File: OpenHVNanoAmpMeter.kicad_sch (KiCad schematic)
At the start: 0 parts

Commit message: updated structure
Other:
- sheet CurrentMeasurement ports: added TIA_IN; removed none
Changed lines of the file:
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@@
 (kicad_sch (version 20211123) (generator eeschema)
   (paper "A4")
-  (sheet (at 154.94 67.31) (size 73.66 34.29) (fields_autoplaced)
+  (sheet (at 50.8 50.8) (size 29.21 34.29) (fields_autoplaced)
     (stroke (width 0.1524) (type solid) (color 0 0 0 0))
     (fill (color 0 0 0 0.0000))
-    (property "Sheet name" "CurrentMeasurement" (id 0) (at 154.94 66.5984 0)
+    (property "Sheet name" "CurrentMeasurement" (id 0) (at 50.8 50.0884 0)
       (effects (font (size 1.27 1.27)) (justify left bottom))
     )
-    (property "Sheet file" "CurrentMeasurement.kicad_sch" (id 1) (at 154.94 102.1846 0)
+    (property "Sheet file" "CurrentMeasurement.kicad_sch" (id 1) (at 50.8 85.6746 0)
       (effects (font (size 1.27 1.27)) (justify left top) hide)
+    )
+    (pin "TIA_IN" input (at 50.8 59.69 180)
+      (effects (font (size 1.27 1.27)) (justify left))
     )
   )
@@
     )
     (property "Sheet file" "InterfacePCside.kicad_sch" (id 1) (at 22.86 36.1446 0)
-      (effects (font (size 1.27 1.27)) (justify left top))
+      (effects (font (size 1.27 1.27)) (justify left top) hide)
     )
   )
-  (sheet (at 105.41 64.77) (size 24.13 41.91) (fields_autoplaced)
+  (sheet (at 87.63 50.8) (size 24.13 34.29) (fields_autoplaced)
     (stroke (width 0.1524) (type solid) (color 0 0 0 0))
     (fill (color 0 0 0 0.0000))
-    (property "Sheet name" "DataProcessing" (id 0) (at 105.41 64.0584 0)
+    (property "Sheet name" "DataProcessing" (id 0) (at 87.63 50.0884 0)
       (effects (font (size 1.27 1.27)) (justify left bottom))
     )
-    (property "Sheet file" "DataProcessing.kicad_sch" (id 1) (at 105.41 107.2646 0)
-      (effects (font (size 1.27 1.27)) (justify left top))
+    (property "Sheet file" "DataProcessing.kicad_sch" (id 1) (at 87.63 85.6746 0)
+      (effects (font (size 1.27 1.27)) (justify left top) hide)
     )
   )
-  (sheet (at 69.85 66.04) (size 27.94 30.48) (fields_autoplaced)
+  (sheet (at 119.38 50.8) (size 27.94 34.29) (fields_autoplaced)
     (stroke (width 0.1524) (type solid) (color 0 0 0 0))
     (fill (color 0 0 0 0.0000))
-    (property "Sheet name" "Interface" (id 0) (at 69.85 65.3284 0)
+    (property "Sheet name" "Interface" (id 0) (at 119.38 50.0884 0)
       (effects (font (size 1.27 1.27)) (justify left bottom))
     )
-    (property "Sheet file" "Interface.kicad_sch" (id 1) (at 69.85 97.1046 0)
-      (effects (font (size 1.27 1.27)) (justify left top))
+    (property "Sheet file" "Interface.kicad_sch" (id 1) (at 119.38 85.6746 0)
+      (effects (font (size 1.27 1.27)) (justify left top) hide)
     )
   )
@@
   )
   (symbol_instances
+    (path "/1a416e56-70b9-4536-9e9f-d6906909692e/55690313-1407-4934-afe0-4c27694f0ce2"
+      (reference "#PWR?") (unit 1) (value "GND1") (footprint "")
+    )
+    (path "/1a416e56-70b9-4536-9e9f-d6906909692e/2dff8e7c-3323-45f1-b4d6-142a477025b9"
+      (reference "C?") (unit 1) (value "C") (footprint "")
+    )
+    (path "/1a416e56-70b9-4536-9e9f-d6906909692e/7952f13c-ca8e-4d9a-ae66-7db9acc3a740"
+      (reference "R?") (unit 1) (value "R") (footprint "")
+    )
     (path "/1a416e56-70b9-4536-9e9f-d6906909692e/7889dd03-e008-429e-85c1-51a59a2503fb"
       (reference "U?") (unit 1) (value "TLC272") (footprint "")
     )
-    (path "/1a416e56-70b9-4536-9e9f-d6906909692e/fbe6d585-7b11-4a8d-a098-4cf5a74e9a83"
-      (reference "U?") (unit 2) (value "TLC272") (footprint "")
-    )
     (path "/1a416e56-70b9-4536-9e9f-d6906909692e/d047c0e9-8f92-47b0-ac3f-1065bf5fbcc0"

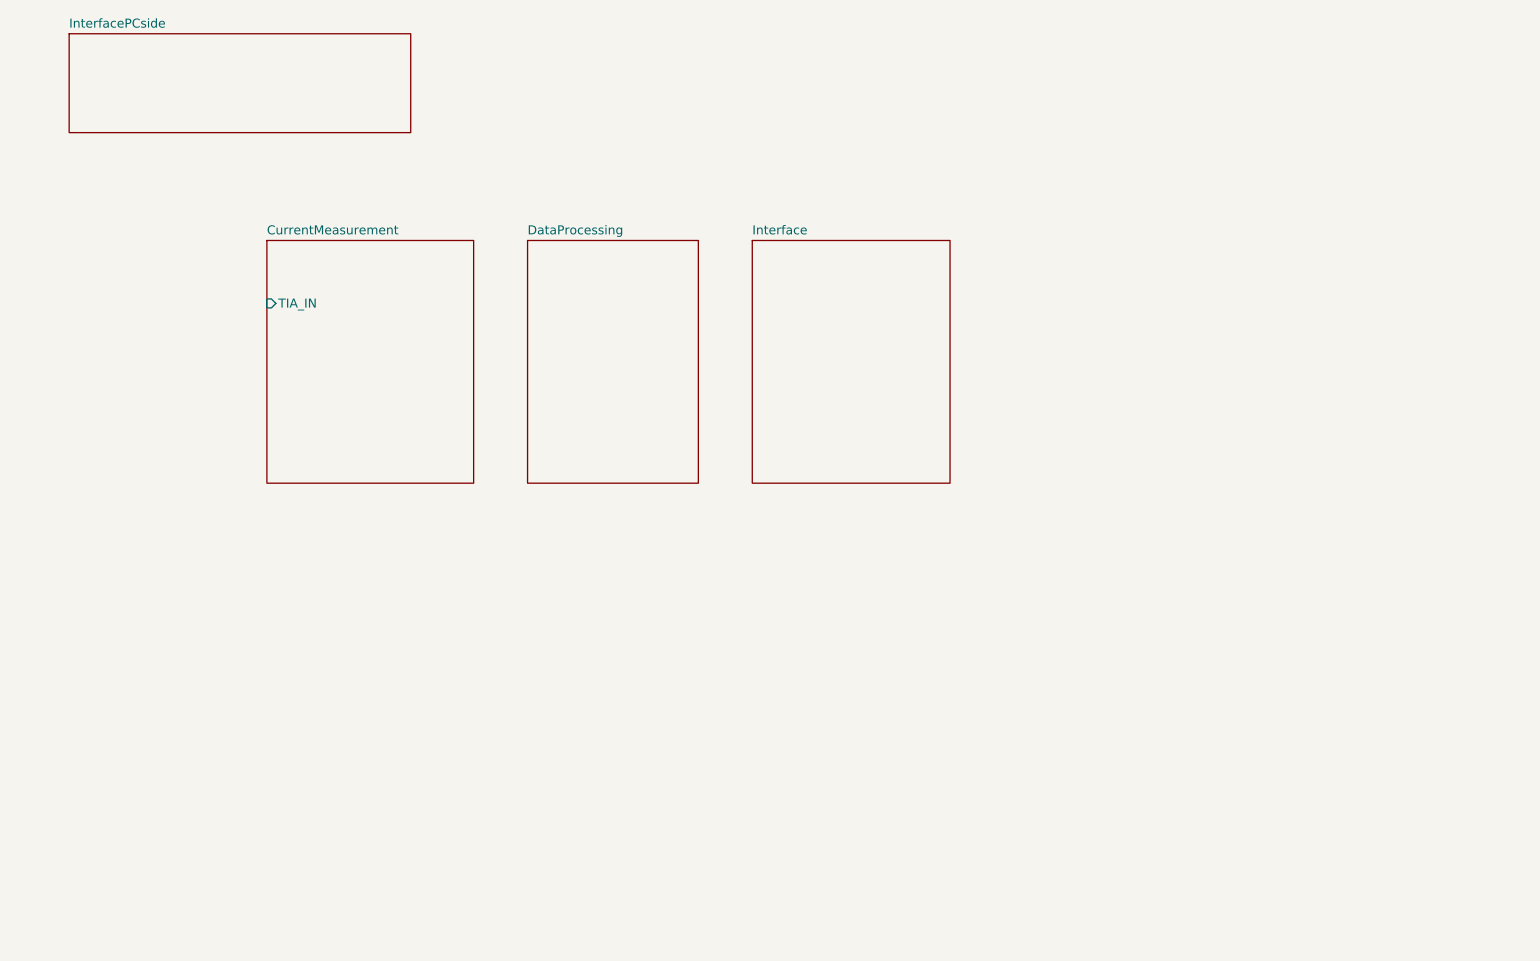
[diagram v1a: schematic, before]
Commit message: added hierachical ports to sheet
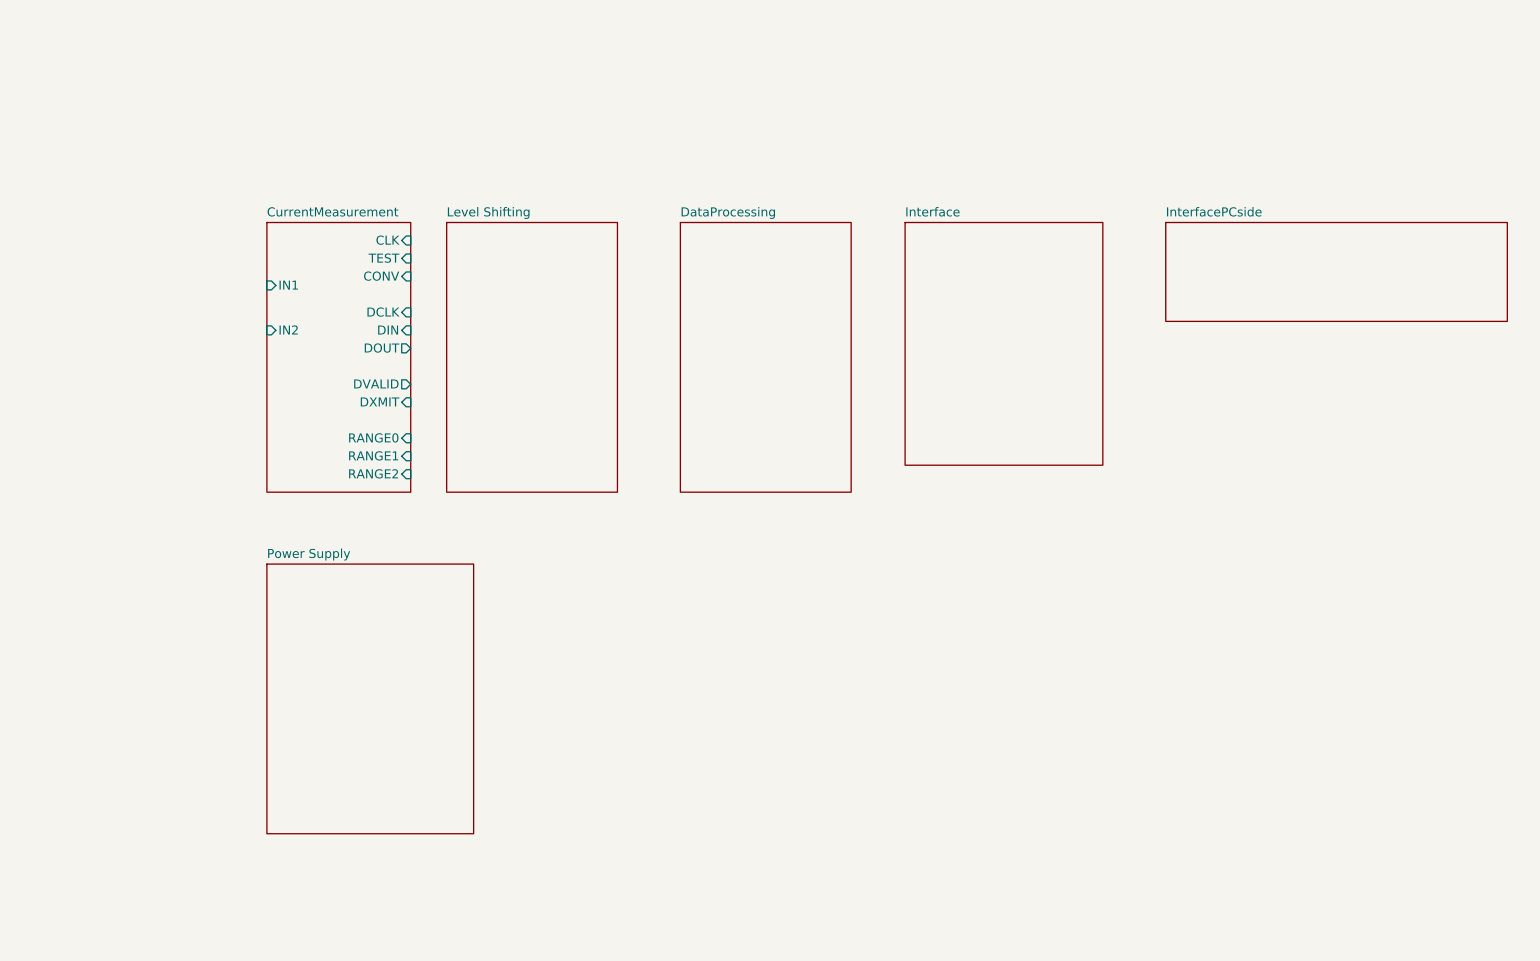
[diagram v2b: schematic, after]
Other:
- added sheet Level Shifting (LevelShift.kicad_sch)
- added sheet Power Supply (powersupply.kicad_sch)
- sheet CurrentMeasurement ports: added CLK, CONV, DCLK, DIN, DOUT, DVALID, DXMIT, IN1, IN2, RANGE0, RANGE1, RANGE2, TEST; removed TIA_IN
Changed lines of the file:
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@@
 (kicad_sch (version 20211123) (generator eeschema)
   (paper "A4")
-  (sheet (at 50.8 50.8) (size 29.21 34.29) (fields_autoplaced)
+  (sheet (at 50.8 48.26) (size 20.32 38.1) (fields_autoplaced)
     (stroke (width 0.1524) (type solid) (color 0 0 0 0))
     (fill (color 0 0 0 0.0000))
-    (property "Sheet name" "CurrentMeasurement" (id 0) (at 50.8 50.0884 0)
+    (property "Sheet name" "CurrentMeasurement" (id 0) (at 50.8 47.5484 0)
       (effects (font (size 1.27 1.27)) (justify left bottom))
     )
-    (property "Sheet file" "CurrentMeasurement.kicad_sch" (id 1) (at 50.8 85.6746 0)
+    (property "Sheet file" "CurrentMeasurement.kicad_sch" (id 1) (at 50.8 86.9446 0)
       (effects (font (size 1.27 1.27)) (justify left top) hide)
     )
-    (pin "TIA_IN" input (at 50.8 59.69 180)
+    (pin "TEST" input (at 71.12 53.34 0)
+      (effects (font (size 1.27 1.27)) (justify right))
+    )
+    (pin "RANGE0" input (at 71.12 78.74 0)
+      (effects (font (size 1.27 1.27)) (justify right))
+    )
+    (pin "CONV" input (at 71.12 55.88 0)
+      (effects (font (size 1.27 1.27)) (justify right))
+    )
+    (pin "RANGE2" input (at 71.12 83.82 0)
+      (effects (font (size 1.27 1.27)) (justify right))
+    )
+    (pin "RANGE1" input (at 71.12 81.28 0)
+      (effects (font (size 1.27 1.27)) (justify right))
+    )
+    (pin "CLK" input (at 71.12 50.8 0)
+      (effects (font (size 1.27 1.27)) (justify right))
+    )
+    (pin "DOUT" output (at 71.12 66.04 0)
+      (effects (font (size 1.27 1.27)) (justify right))
+    )
+    (pin "DCLK" input (at 71.12 60.96 0)
+      (effects (font (size 1.27 1.27)) (justify right))
+    )
+    (pin "DXMIT" input (at 71.12 73.66 0)
+      (effects (font (size 1.27 1.27)) (justify right))
+    )
+    (pin "DVALID" output (at 71.12 71.12 0)
+      (effects (font (size 1.27 1.27)) (justify right))
+    )
+    (pin "DIN" input (at 71.12 63.5 0)
+      (effects (font (size 1.27 1.27)) (justify right))
+    )
+    (pin "IN1" input (at 50.8 57.15 180)
+      (effects (font (size 1.27 1.27)) (justify left))
+    )
+    (pin "IN2" input (at 50.8 63.5 180)
       (effects (font (size 1.27 1.27)) (justify left))
     )
   )
-  (sheet (at 22.86 21.59) (size 48.26 13.97) (fields_autoplaced)
+  (sheet (at 76.2 48.26) (size 24.13 38.1) (fields_autoplaced)
     (stroke (width 0.1524) (type solid) (color 0 0 0 0))
     (fill (color 0 0 0 0.0000))
-    (property "Sheet name" "InterfacePCside" (id 0) (at 22.86 20.8784 0)
+    (property "Sheet name" "Level Shifting" (id 0) (at 76.2 47.5484 0)
       (effects (font (size 1.27 1.27)) (justify left bottom))
     )
-    (property "Sheet file" "InterfacePCside.kicad_sch" (id 1) (at 22.86 36.1446 0)
+    (property "Sheet file" "LevelShift.kicad_sch" (id 1) (at 76.2 86.9446 0)
       (effects (font (size 1.27 1.27)) (justify left top) hide)
     )
   )
-  (sheet (at 87.63 50.8) (size 24.13 34.29) (fields_autoplaced)
+  (sheet (at 177.8 48.26) (size 48.26 13.97) (fields_autoplaced)
     (stroke (width 0.1524) (type solid) (color 0 0 0 0))
     (fill (color 0 0 0 0.0000))
-    (property "Sheet name" "DataProcessing" (id 0) (at 87.63 50.0884 0)
+    (property "Sheet name" "InterfacePCside" (id 0) (at 177.8 47.5484 0)
       (effects (font (size 1.27 1.27)) (justify left bottom))
     )
-    (property "Sheet file" "DataProcessing.kicad_sch" (id 1) (at 87.63 85.6746 0)
+    (property "Sheet file" "InterfacePCside.kicad_sch" (id 1) (at 177.8 62.8146 0)
       (effects (font (size 1.27 1.27)) (justify left top) hide)
     )
   )
-  (sheet (at 119.38 50.8) (size 27.94 34.29) (fields_autoplaced)
+  (sheet (at 109.22 48.26) (size 24.13 38.1) (fields_autoplaced)
     (stroke (width 0.1524) (type solid) (color 0 0 0 0))
     (fill (color 0 0 0 0.0000))
-    (property "Sheet name" "Interface" (id 0) (at 119.38 50.0884 0)
+    (property "Sheet name" "DataProcessing" (id 0) (at 109.22 47.5484 0)
       (effects (font (size 1.27 1.27)) (justify left bottom))
     )
-    (property "Sheet file" "Interface.kicad_sch" (id 1) (at 119.38 85.6746 0)
+    (property "Sheet file" "DataProcessing.kicad_sch" (id 1) (at 109.22 86.9446 0)
+      (effects (font (size 1.27 1.27)) (justify left top) hide)
+    )
+  )
+  (sheet (at 140.97 48.26) (size 27.94 34.29) (fields_autoplaced)
+    (stroke (width 0.1524) (type solid) (color 0 0 0 0))
+    (fill (color 0 0 0 0.0000))
+    (property "Sheet name" "Interface" (id 0) (at 140.97 47.5484 0)
+      (effects (font (size 1.27 1.27)) (justify left bottom))
+    )
+    (property "Sheet file" "Interface.kicad_sch" (id 1) (at 140.97 83.1346 0)
+      (effects (font (size 1.27 1.27)) (justify left top) hide)
+    )
+  )
+  (sheet (at 50.8 96.52) (size 29.21 38.1) (fields_autoplaced)
+    (stroke (width 0.1524) (type solid) (color 0 0 0 0))
+    (fill (color 0 0 0 0.0000))
+    (property "Sheet name" "Power Supply" (id 0) (at 50.8 95.8084 0)
+      (effects (font (size 1.27 1.27)) (justify left bottom))
+    )
+    (property "Sheet file" "powersupply.kicad_sch" (id 1) (at 50.8 135.2046 0)
       (effects (font (size 1.27 1.27)) (justify left top) hide)
     )
@@
     (path "/b1489b53-6bfd-484b-944a-0c1d055adf37" (page "4"))
     (path "/58e2bd5c-58d1-4db2-9f48-6c5d4d73d3a1" (page "5"))
+    (path "/d7b74773-6757-4dce-9b74-0ca53265265a" (page "6"))
+    (path "/4c5a28c9-51e7-4865-9f3a-eb3389efc1d0" (page "7"))
   )
   (symbol_instances
-    (path "/1a416e56-70b9-4536-9e9f-d6906909692e/55690313-1407-4934-afe0-4c27694f0ce2"
-      (reference "#PWR?") (unit 1) (value "GND1") (footprint "")
+    (path "/1a416e56-70b9-4536-9e9f-d6906909692e/c05f9092-0414-4fb2-84f5-deb77d878292"
+      (reference "#PWR0101") (unit 1) (value "GND") (footprint "")
     )
-    (path "/1a416e56-70b9-4536-9e9f-d6906909692e/2dff8e7c-3323-45f1-b4d6-142a477025b9"
-      (reference "C?") (unit 1) (value "C") (footprint "")
+    (path "/1a416e56-70b9-4536-9e9f-d6906909692e/66cd8d7f-4790-4899-b38f-938d863ef6a1"
+      (reference "#PWR0102") (unit 1) (value "GNDA") (footprint "")
     )
-    (path "/1a416e56-70b9-4536-9e9f-d6906909692e/7952f13c-ca8e-4d9a-ae66-7db9acc3a740"
+    (path "/d7b74773-6757-4dce-9b74-0ca53265265a/33c862ab-9c71-49cd-a74d-2719b960e38d"
+      (reference "BT1") (unit 1) (value "9V") (footprint "Battery:BatteryHolder_MPD_BA9VPC_1xPP3")
+    )
+    (path "/d7b74773-6757-4dce-9b74-0ca53265265a/272a8ace-9060-4b79-8e0b-26b10d64eddf"
+      (reference "BT2") (unit 1) (value "9V") (footprint "Battery:BatteryHolder_MPD_BA9VPC_1xPP3")
+    )
+    (path "/1a416e56-70b9-4536-9e9f-d6906909692e/fde68567-8c9c-41e9-b188-08fc9d33e579"
+      (reference "C1") (unit 1) (value "100p") (footprint "Capacitor_SMD:C_0402_1005Metric_Pad0.74x0.62mm_HandSolder")
+    )
+    (path "/1a416e56-70b9-4536-9e9f-d6906909692e/1a25d881-59d0-439e-b568-e31973d5aa0b"
+      (reference "C2") (unit 1) (value "100p") (footprint "Capacitor_SMD:C_0402_1005Metric_Pad0.74x0.62mm_HandSolder")
+    )
+    (path "/1a416e56-70b9-4536-9e9f-d6906909692e/07538b7e-12bc-4746-bfb2-e2c595ef9816"
+      (reference "C3") (unit 1) (value "100p") (footprint "Capacitor_SMD:C_0402_1005Metric_Pad0.74x0.62mm_HandSolder")
+    )
+    (path "/1a416e56-70b9-4536-9e9f-d6906909692e/6c2c8ac5-6c59-4698-a132-98f9960d7de3"
+      (reference "C4") (unit 1) (value "100p") (footprint "Capacitor_SMD:C_0402_1005Metric_Pad0.74x0.62mm_HandSolder")
+    )
+    (path "/1a416e56-70b9-4536-9e9f-d6906909692e/44100ad1-4967-4847-b004-f8583ab8d1c5"
       (reference "R?") (unit 1) (value "R") (footprint "")
     )
-    (path "/1a416e56-70b9-4536-9e9f-d6906909692e/7889dd03-e008-429e-85c1-51a59a2503fb"
-      (reference "U?") (unit 1) (value "TLC272") (footprint "")
+    (path "/1a416e56-70b9-4536-9e9f-d6906909692e/c0fb7dd7-4a21-4545-8078-d2e868c456af"
+      (reference "R?") (unit 1) (value "R") (footprint "")
     )
-    (path "/1a416e56-70b9-4536-9e9f-d6906909692e/d047c0e9-8f92-47b0-ac3f-1065bf5fbcc0"
-      (reference "U?") (unit 3) (value "TLC272") (footprint "")
+    (path "/1a416e56-70b9-4536-9e9f-d6906909692e/8545a50e-7da1-4f47-95c3-a84b8f7a0500"
+      (reference "U1") (unit 1) (value "DDC112U") (footprint "Package_SO:SOIC-28W_7.5x17.9mm_P1.27mm")
+    )
+    (path "/1a416e56-70b9-4536-9e9f-d6906909692e/2ec0ca8f-749e-44b7-a771-6bc6852a39b5"
+      (reference "U1") (unit 2) (value "DDC112U") (footprint "Package_SO:SOIC-28W_7.5x17.9mm_P1.27mm")
+    )
+    (path "/1a416e56-70b9-4536-9e9f-d6906909692e/63dace22-7b01-4468-86e6-e4cbd05f9b8c"
+      (reference "U1") (unit 3) (value "DDC112U") (footprint "Package_SO:SOIC-28W_7.5x17.9mm_P1.27mm")
+    )
+    (path "/1a416e56-70b9-4536-9e9f-d6906909692e/39dc6e3e-fc57-47a5-9217-89d2962a52c7"
+      (reference "U1") (unit 4) (value "DDC112U") (footprint "Package_SO:SOIC-28W_7.5x17.9mm_P1.27mm")
     )
   )

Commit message: added coax connectors as input
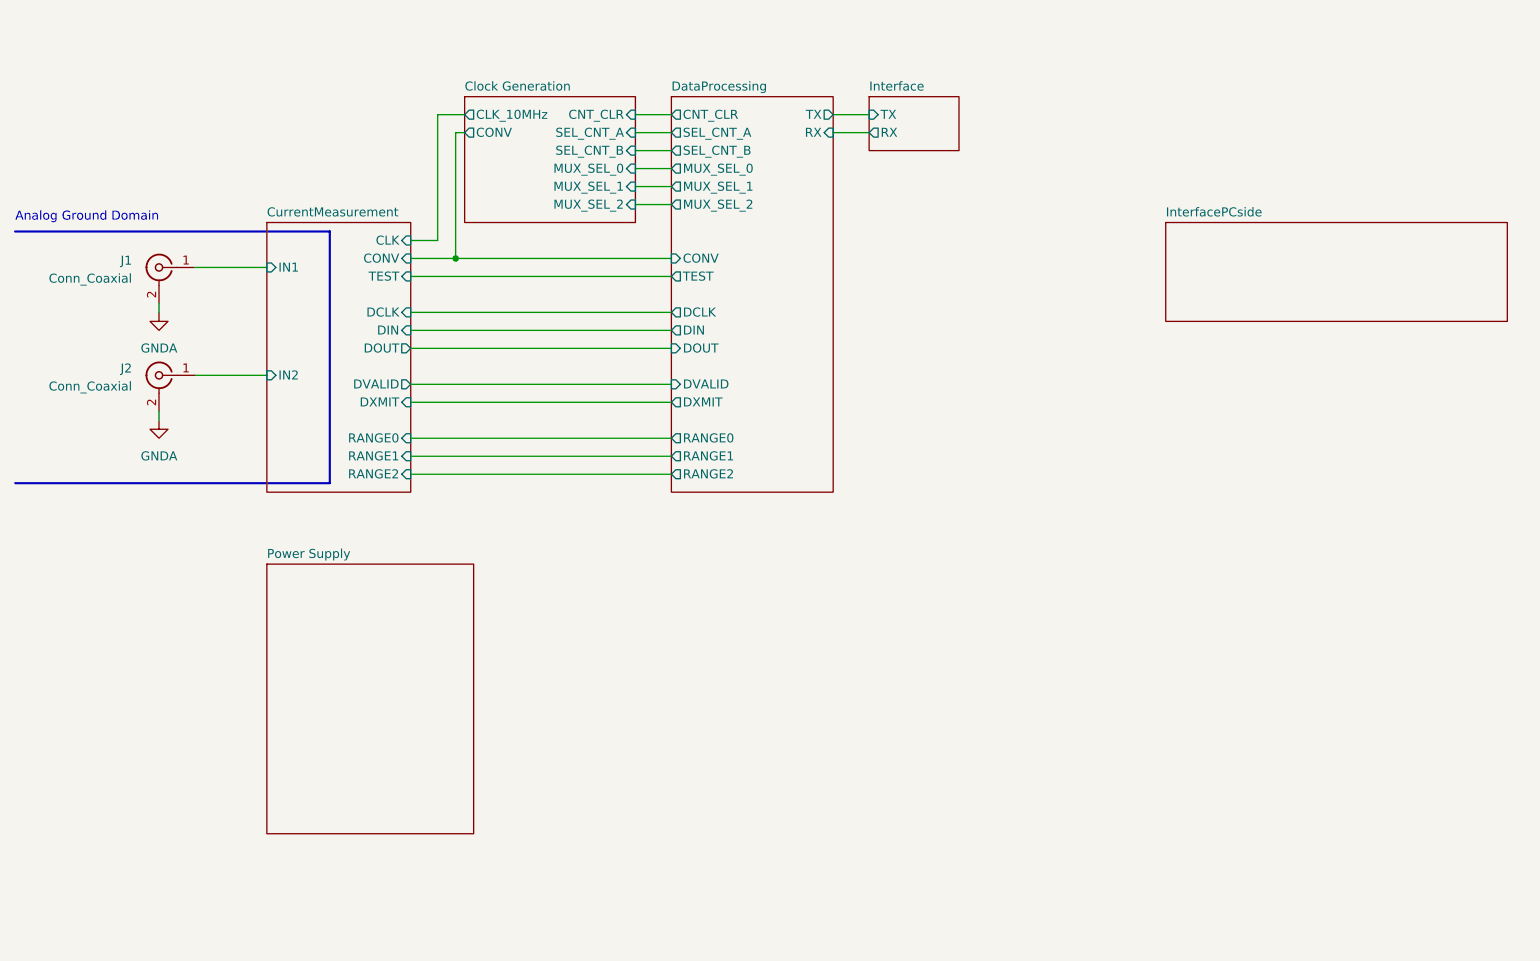
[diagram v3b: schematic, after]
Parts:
- added J1, J2: Conn_Coaxial, Connector_Coaxial:SMA_Amphenol_132289_EdgeMount, symbol Connector:Conn_Coaxial
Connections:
- net CurrentMeasurement/IN1: now also J1.1 (In)
- net CurrentMeasurement/IN2: now also J2.1 (In)
- new net GNDA: J1.2 (Ext), J2.2 (Ext)
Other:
- removed sheet Level Shifting
- added sheet Clock Generation (Clock_10MHz.kicad_sch)
- sheet DataProcessing ports: added CNT_CLR, CONV, DCLK, DIN, DOUT, DVALID, DXMIT, MUX_SEL_0, MUX_SEL_1, MUX_SEL_2, RANGE0, RANGE1, RANGE2, RX, SEL_CNT_A, SEL_CNT_B, TEST, TX; removed none
- sheet Interface ports: added RX, TX; removed none
- note added: "Analog Ground Domain"

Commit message: small project updates
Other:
- sheet DataProcessing ports: added none; removed DIN

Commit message: changed title block to meaningful information
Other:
- title: (none) -> Open Nano Amp Meter
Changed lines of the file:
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@@
 (kicad_sch (version 20211123) (generator eeschema)
   (paper "A4")
+  (title_block
+    (title "Open Nano Amp Meter")
+    (date "2022-11-17")
+    (rev "0.9")
+  )
   (junction (at 77.47 53.34) (diameter 0) (color 0 0 0 0)
   )
